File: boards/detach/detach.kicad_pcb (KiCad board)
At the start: 2 copper layers, 304.9 x 114.5 mm, 180 parts, among them J1 AVR-ISP-6, SW0 KEYSW, SW1 KEYSW, SW10 KEYSW, SW11 KEYSW, SW12 KEYSW, SW13 KEYSW, SW14 KEYSW, SW15 KEYSW, SW16 KEYSW, SW17 KEYSW, SW18 KEYSW, SW19 KEYSW, SW2 KEYSW, SW20 KEYSW, SW21 KEYSW, SW22 KEYSW, SW23 KEYSW, SW24 KEYSW, SW25 KEYSW, SW26 KEYSW, SW27 KEYSW, SW28 KEYSW, SW29 KEYSW, SW3 KEYSW, SW30 KEYSW, SW31 KEYSW, SW32 KEYSW, SW33 KEYSW, SW34 KEYSW, SW35 KEYSW, SW36 KEYSW, SW37 KEYSW, SW38 KEYSW, SW39 KEYSW, SW4 KEYSW, SW40 KEYSW, SW41 KEYSW, SW42 KEYSW, SW43 KEYSW, SW44 KEYSW, SW46 KEYSW, SW47 KEYSW, SW48 KEYSW, SW49 KEYSW, SW5 KEYSW, SW50 KEYSW, SW51 KEYSW, SW52 KEYSW, SW53 KEYSW, SW54 KEYSW, SW55 KEYSW, SW56 KEYSW, SW57 KEYSW, SW58 KEYSW, SW59 KEYSW, SW6 KEYSW, SW60 KEYSW, SW61 KEYSW, SW62 KEYSW, SW63 KEYSW, SW64 KEYSW, SW65 KEYSW, SW66 KEYSW, SW67 KEYSW, SW68 KEYSW, SW69 KEYSW, SW7 KEYSW, SW8 KEYSW, SW9 KEYSW, U1 ATmega32A-PU, Y1 Crystal

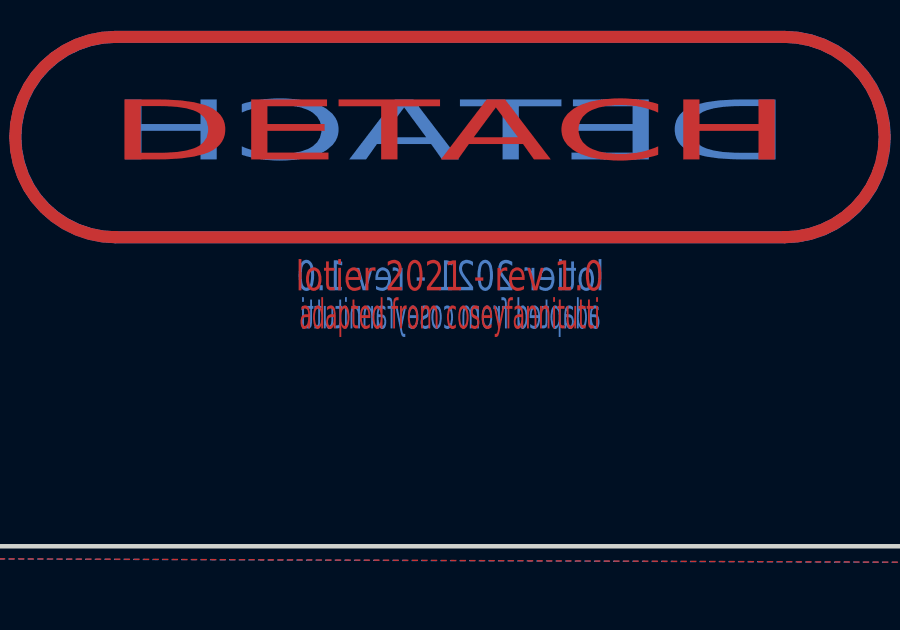
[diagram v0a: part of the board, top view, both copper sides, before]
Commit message: Reorg of project layout
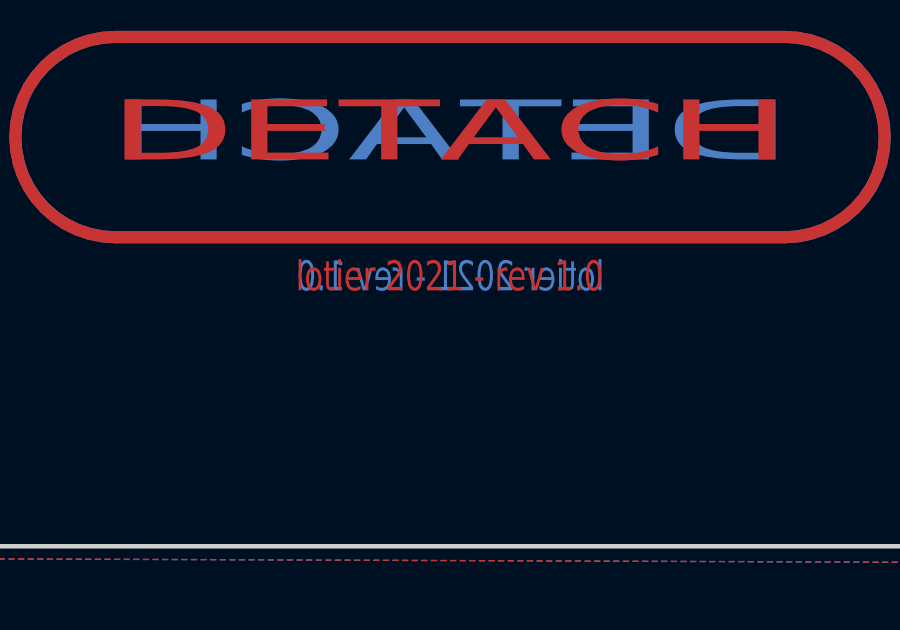
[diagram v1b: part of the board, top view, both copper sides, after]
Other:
- board text added: "DETACH - 65% hotswap keyboard assembled with through hole components (ANSI)"
- board text removed: "DELIGHT - 65% keyboard assembled with only through hole components"
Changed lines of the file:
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@@
     (34 B.Paste user hide)
     (35 F.Paste user hide)
-    (36 B.SilkS user hide)
+    (36 B.SilkS user)
     (37 F.SilkS user)
-    (38 B.Mask user hide)
-    (39 F.Mask user hide)
+    (38 B.Mask user)
+    (39 F.Mask user)
     (40 Dwgs.User user hide)
     (41 Cmts.User user hide)
@@
     (add_net row4)
   )
-  (module Lotier:DETACH_SMALL (layer B.Cu)
-    (at 163.831144 178.11221 180)
-    (fp_text reference G*** (at 0 0) (layer B.SilkS) hide
-      (effects (font (size 1.524 1.524) (thickness 0.3)) (justify mirror))
-    )
-    (fp_text value LOGO (at 0.75 0) (layer B.SilkS) hide
-      (effects (font (size 1.524 1.524) (thickness 0.3)) (justify mirror))
-    )
-    (fp_text user DELIGHT (at 0 0) (layer B.Mask)
-      (effects (font (size 2 4) (thickness 0.35)) (justify mirror))
-    )
-    (fp_text user "lotier 2021 - rev 1.0" (at 0 -4.826) (layer B.Mask)
-      (effects (font (size 1 0.75) (thickness 0.125)) (justify mirror))
-    )
-    (fp_text user "lotier 2021 - rev 1.0" (at 0 -4.826) (layer B.Cu)
-      (effects (font (size 1 0.75) (thickness 0.125)) (justify mirror))
-    )
-    (fp_text user "adapted from coseyfannitutti" (at 0 -6.096) (layer B.Cu)
-      (effects (font (size 1 0.5) (thickness 0.125)) (justify mirror))
-    )
-    (fp_text user "adapted from coseyfannitutti" (at 0 -6.096) (layer B.Mask)
-      (effects (font (size 1 0.5) (thickness 0.125)) (justify mirror))
-    )
-    (fp_arc (start -11.14 -0.18) (end -11.14 3.16) (angle 180) (layer B.Cu) (width 0.4))
-    (fp_arc (start 11.16 -0.18) (end 11.16 -3.52) (angle 180) (layer B.Mask) (width 0.4))
-    (fp_arc (start -11.14 -0.18) (end -11.14 3.16) (angle 180) (layer B.Mask) (width 0.4))
-    (fp_arc (start 11.16 -0.18) (end 11.16 -3.52) (angle 180) (layer B.Cu) (width 0.4))
-    (fp_text user DETACH (at 0 0) (layer B.Mask)
-      (effects (font (size 2 4) (thickness 0.35)) (justify mirror))
-    )
-    (fp_text user DETACH (at 0 0) (layer B.Cu)
-      (effects (font (size 2 4) (thickness 0.35)) (justify mirror))
-    )
-    (fp_line (start -11.13 -3.52) (end 11.17 -3.52) (layer B.Mask) (width 0.4))
-    (fp_line (start -11.11 3.16) (end 11.17 3.16) (layer B.Cu) (width 0.4))
-    (fp_line (start -11.13 -3.52) (end 11.17 -3.52) (layer B.Cu) (width 0.4))
-    (fp_line (start -11.11 3.16) (end 11.17 3.16) (layer B.Mask) (width 0.4))
-  )
   (module Lotier:DETACH_SMALL (layer F.Cu)
     (at 163.803456 178.11221)
@@
       (effects (font (size 1.524 1.524) (thickness 0.3)))
     )
+    (fp_line (start -11.13 3.52) (end 11.17 3.52) (layer F.Mask) (width 0.4))
+    (fp_line (start -11.11 -3.16) (end 11.17 -3.16) (layer F.Cu) (width 0.4))
+    (fp_line (start -11.13 3.52) (end 11.17 3.52) (layer F.Cu) (width 0.4))
+    (fp_line (start -11.11 -3.16) (end 11.17 -3.16) (layer F.Mask) (width 0.4))
     (fp_text user "lotier 2021 - rev 1.0" (at 0 4.826) (layer F.Mask)
       (effects (font (size 1 0.75) (thickness 0.125)))
@@
       (effects (font (size 1 0.75) (thickness 0.125)))
     )
-    (fp_text user "adapted from coseyfannitutti" (at 0 6.096) (layer F.Cu)
-      (effects (font (size 1 0.5) (thickness 0.125)))
-    )
-    (fp_text user "adapted from coseyfannitutti" (at 0 6.096) (layer F.Mask)
-      (effects (font (size 1 0.5) (thickness 0.125)))
-    )
     (fp_arc (start -11.14 0.18) (end -11.14 -3.16) (angle -180) (layer F.Cu) (width 0.4))
     (fp_arc (start 11.16 0.18) (end 11.16 3.52) (angle -180) (layer F.Mask) (width 0.4))
@@
       (effects (font (size 2 4) (thickness 0.35)))
     )
-    (fp_line (start -11.13 3.52) (end 11.17 3.52) (layer F.Mask) (width 0.4))
-    (fp_line (start -11.11 -3.16) (end 11.17 -3.16) (layer F.Cu) (width 0.4))
-    (fp_line (start -11.13 3.52) (end 11.17 3.52) (layer F.Cu) (width 0.4))
-    (fp_line (start -11.11 -3.16) (end 11.17 -3.16) (layer F.Mask) (width 0.4))
+  )
+  (module Lotier:DETACH_SMALL (layer B.Cu)
+    (at 163.831144 178.11221 180)
+    (fp_text reference G*** (at 0 0) (layer B.SilkS) hide
+      (effects (font (size 1.524 1.524) (thickness 0.3)) (justify mirror))
+    )
+    (fp_text value LOGO (at 0.75 0) (layer B.SilkS) hide
+      (effects (font (size 1.524 1.524) (thickness 0.3)) (justify mirror))
+    )
+    (fp_line (start -11.13 -3.52) (end 11.17 -3.52) (layer B.Mask) (width 0.4))
+    (fp_line (start -11.11 3.16) (end 11.17 3.16) (layer B.Cu) (width 0.4))
+    (fp_line (start -11.13 -3.52) (end 11.17 -3.52) (layer B.Cu) (width 0.4))
+    (fp_line (start -11.11 3.16) (end 11.17 3.16) (layer B.Mask) (width 0.4))
+    (fp_text user "lotier 2021 - rev 1.0" (at 0 -4.826) (layer B.Mask)
+      (effects (font (size 1 0.75) (thickness 0.125)) (justify mirror))
+    )
+    (fp_text user "lotier 2021 - rev 1.0" (at 0 -4.826) (layer B.Cu)
+      (effects (font (size 1 0.75) (thickness 0.125)) (justify mirror))
+    )
+    (fp_arc (start -11.14 -0.18) (end -11.14 3.16) (angle 180) (layer B.Cu) (width 0.4))
+    (fp_arc (start 11.16 -0.18) (end 11.16 -3.52) (angle 180) (layer B.Mask) (width 0.4))
+    (fp_arc (start -11.14 -0.18) (end -11.14 3.16) (angle 180) (layer B.Mask) (width 0.4))
+    (fp_arc (start 11.16 -0.18) (end 11.16 -3.52) (angle 180) (layer B.Cu) (width 0.4))
+    (fp_text user DETACH (at 0 0) (layer B.Mask)
+      (effects (font (size 2 4) (thickness 0.35)) (justify mirror))
+    )
+    (fp_text user DETACH (at 0 0) (layer B.Cu)
+      (effects (font (size 2 4) (thickness 0.35)) (justify mirror))
+    )
   )
   (module Switch_Keyboard_Kailh:SW_Hotswap_Kailh_1.00u (layer F.Cu)
@@
     (effects (font (size 1.5 1.5) (thickness 0.3)))
   )
-  (gr_text "DELIGHT - 65% keyboard assembled with only through hole components" (at 353.4156 261.2644) (layer Cmts.User)
+  (gr_text "DETACH - 65% hotswap keyboard assembled with through hole components (ANSI)" (at 353.4156 261.2644) (layer Cmts.User)
     (effects (font (size 1.5 1.5) (thickness 0.3)))
   )
@@
     (effects (font (size 1.5 1.5) (thickness 0.3)))
   )
-  (gr_text "DELIGHT - 65% keyboard assembled with only through hole components" (at 364.3376 272.6944) (layer Cmts.User)
+  (gr_text "DETACH - 65% hotswap keyboard assembled with through hole components (ANSI)" (at 364.3376 272.6944) (layer Cmts.User)
     (effects (font (size 1.5 1.5) (thickness 0.3)))
   )

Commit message: Fixed up 3D reference for stabilizers
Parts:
- ST13, ST42, ST59: footprint stabs:Stabilizer_Cherry_MX_2u -> Mounting_Keyboard:Stabilizer_Cherry_MX_2u
- ST63: footprint stabs:Stabilizer_Cherry_MX_6.25u -> Mounting_Keyboard:Stabilizer_Cherry_MX_6.25u
